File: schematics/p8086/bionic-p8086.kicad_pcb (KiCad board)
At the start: 2 copper layers, 48.3 x 71.1 mm, 10 parts, among them J1 Bionic-P135, J2 Bionic-P245, U1 P80C86A, U2 74HCT126, U3 11AA010-I/TO

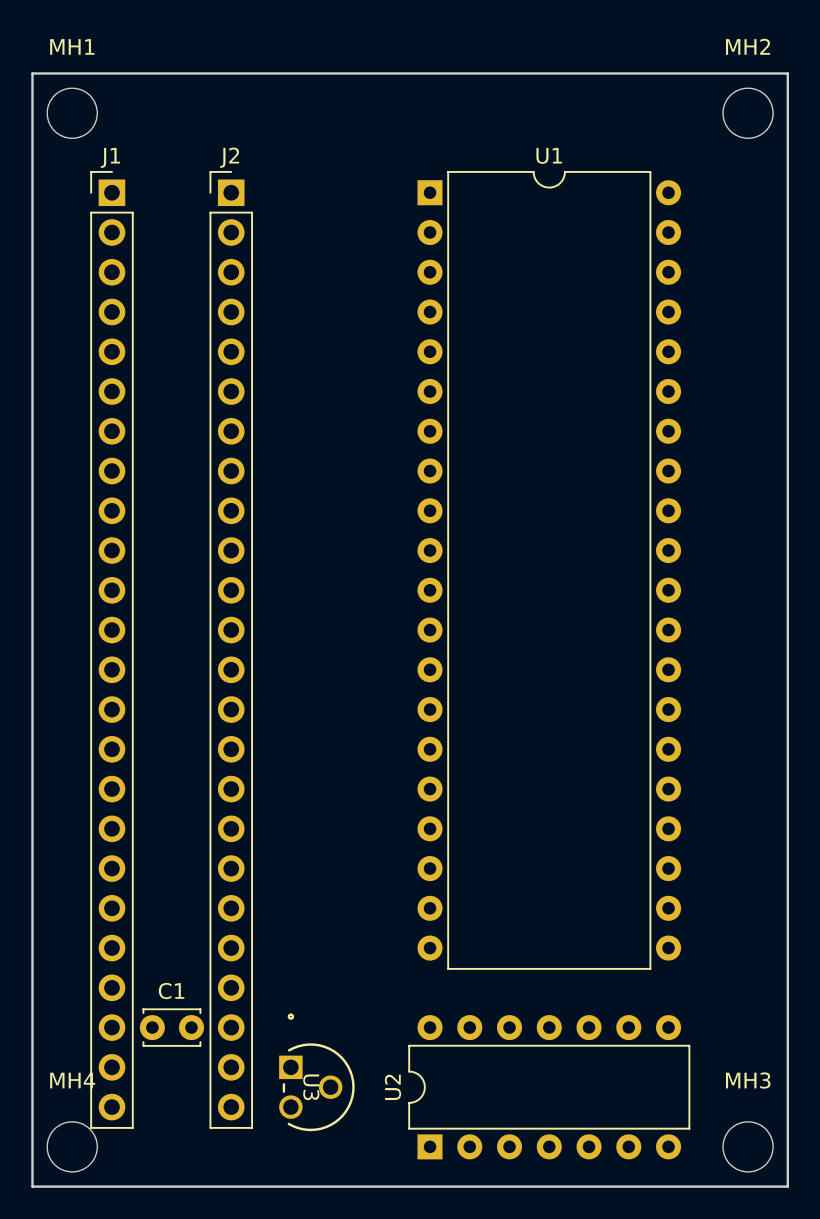
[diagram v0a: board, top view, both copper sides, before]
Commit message: [p8086] Redraw the P8086 board for the Bionic connector pin map
One board for the P8086, P8088, V20 and V30 with no logic ICs; the
8-bit parts are told apart by pin 28's polarity. Routed on two layers.
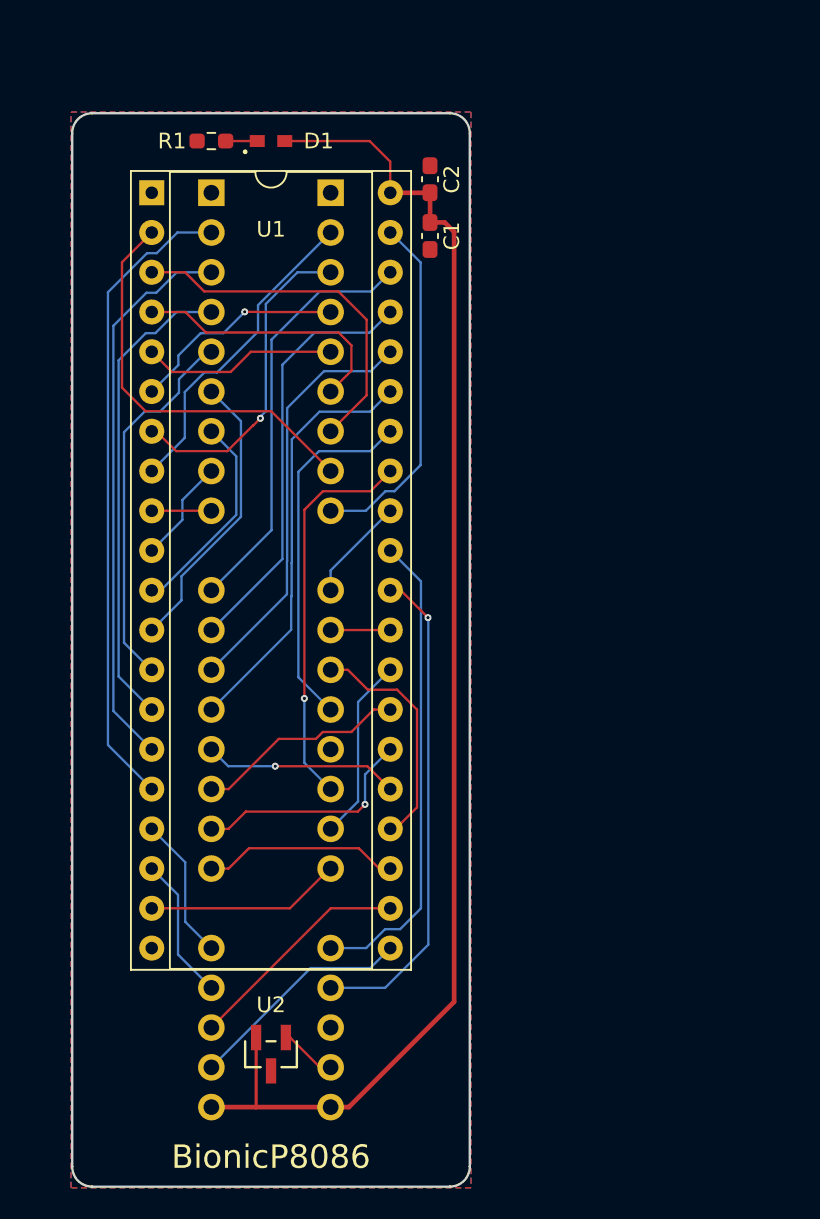
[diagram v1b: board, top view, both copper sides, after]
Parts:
- removed MH1, MH2, MH3, MH4: MountingHole_3.2mm_M3, MountingHole:MountingHole_3.2mm_M3
- removed U3: 11AA010-I/TO, microchip:TO-92_MC_MCH
- added C2: 0.1u, Capacitor_SMD:C_0603_1608Metric_Pad1.08x0.95mm_HandSolder, F.Cu at (123.9, 74.2)
- added D1: CSL1901UW1, rhom:LED_CSL1901UW1_ROM-M, F.Cu at (113.7, 71.8)
- added R1: 1.6k, Resistor_SMD:R_0603_1608Metric_Pad0.98x0.95mm_HandSolder, F.Cu at (109.9, 71.8)
- C1: value 0.1u -> 22u; footprint Capacitor_THT:C_Disc_D3.4mm_W2.1mm_P2.50mm -> Capacitor_SMD:C_0603_1608Metric_Pad1.08x0.95mm_HandSolder
- J1: footprint connector:Bionic-P135_Vertical -> bionic:Bionic-P135_THT; moved to B.Cu
- J2: footprint connector:Bionic-P245_Vertical -> bionic:Bionic-P245_THT; moved to B.Cu
- U1: value P80C86A -> P8086; footprint Package_DIP:DIP-40_W15.24mm -> bionic:DIP-40_W15.24mm_Socket
- U2: value 74HCT126 -> 11AA010-I/TT; footprint Package_DIP:DIP-14_W7.62mm -> microchip:SOT-23_MC_MCH-M
- moved C1 53.6 mm to (123.9, 77.8), turned to -90 degrees
- moved U1 17.8 mm to (106.1, 75.1)
- moved U2 11.8 mm to (113.7, 130.1), turned to 180 degrees
- moved J2 6.35 mm to (117.5, 75.1), turned to 180 degrees
- moved J1 6.35 mm to (109.9, 75.1), turned to 180 degrees
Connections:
- net /P10 renamed AD0
- net /P11 renamed AD1
- net /P12 renamed AD2
- net /P13 renamed AD3
- net /P14 renamed AD4
- net /P15 renamed AD5
- net /P16 renamed AD6
- net /P17 renamed AD7
- net /P20 renamed AD8
- net /P21 renamed AD9
- net /P22 renamed AD10
- net /P23 renamed AD11
- net /P24 renamed AD12
- net /P25 renamed AD13
- net /P26 renamed AD14
- net /P27 renamed AD15
- net /P30 renamed A16
- net /P31 renamed A17
- net /P32 renamed A18
- net /P33 renamed A19
- net /P35 renamed DT/~{R}
- net /P52 renamed READY
- net /P53 renamed RESET
- J1 pad 15: /P34 -> ALE
- J1 pad 17: /P36 -> ~{DEN}
- J1 pad 18: /P37 -> ~{TEST}
- J1 pad 20: /P50 -> NMI
- J1 pad 21: /P51 -> INTR
- J2 pad 28: /P55 -> HLDA
- J2 pad 29: /P54 -> HOLD
- J2 pad 31: /P47 -> CLK
- J2 pad 32: /P46 -> M/~{IO}
- J2 pad 33: unconnected-(J2-P45-Pad33) -> MN/~{MX}
- J2 pad 34: /P44 -> unconnected-(J2-P44-Pad34)
- J2 pad 35: /P43 -> ~{BHE}
- J2 pad 36: /P42 -> ~{INTA}
- J2 pad 37: unconnected-(J2-P41-Pad37) -> ~{WR}
- J2 pad 38: /P40 -> ~{RD}
- U1 pad 17: /P43 -> NMI
- U1 pad 18: /P42 -> INTR
- U1 pad 19: Net-(U1-CLK) -> CLK
- U1 pad 23: VCC -> ~{TEST}
- U1 pad 24: /P54 -> ~{INTA}
- U1 pad 25: /P40 -> ALE
- U1 pad 26: /P44 -> ~{DEN}
- U1 pad 28: /P55 -> M/~{IO}
- U1 pad 29: /P51 -> ~{WR}
- U1 pad 30: /P36 -> HLDA
- U1 pad 31: /P37 -> HOLD
- U1 pad 32: /P50 -> ~{RD}
- U1 pad 33: /P47 -> MN/~{MX}
- U1 pad 34: /P34 -> ~{BHE}
- U2 pad 1: VCC -> Net-(J2-P57)
- U2 pad 2: /P46 -> VCC
- U2 pad 3: Net-(U1-CLK) -> GND
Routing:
- net VCC: track 0.00 -> 87.4 mm
- net AD0: track 0.00 -> 41.1 mm
- net AD1: track 0.00 -> 35.8 mm
- net HLDA: track 0.00 -> 31.4 mm, vias 0 -> 1
- net HOLD: track 0.00 -> 30.5 mm
- net AD2: track 0.00 -> 30.4 mm
- net A17: track 0.00 -> 27.1 mm
- net A16: track 0.00 -> 27.0 mm
- net A19: track 0.00 -> 27.0 mm
- net A18: track 0.00 -> 26.8 mm
- net AD14: track 0.00 -> 26.3 mm
- net MN/~{MX}: track 0.00 -> 25.1 mm, vias 0 -> 1
- net AD3: track 0.00 -> 24.2 mm
- net AD13: track 0.00 -> 23.1 mm
- net ~{BHE}: track 0.00 -> 23.0 mm
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- added copper zone on B.Cu, net GND
- added copper zone on F.Cu, net GND
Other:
- board size 48.3 x 71.1 mm -> 25.4 x 68.6 mm
- rule pad_to_mask_clearance: 0.051 -> 0
- board text added: "BionicP8086"
- board text added: "Rev. 1"
